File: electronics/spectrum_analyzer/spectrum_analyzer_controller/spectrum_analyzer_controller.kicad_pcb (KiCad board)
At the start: 2 copper layers, 99.1 x 66 mm, 50 parts, among them J1 AudioJack3, J2 Conn_02x03_Odd_Even, J3 Barrel_Jack_Switch, J4 Conn_01x10_Socket, J5 Conn_01x14_Socket, SW1 SW_SPDT, U1 MSGEQ7 MSGEQ7, U2 MSGEQ7 MSGEQ7, U3 ATtiny84 ATtiny84-20P, U4 74HC595 74HC595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

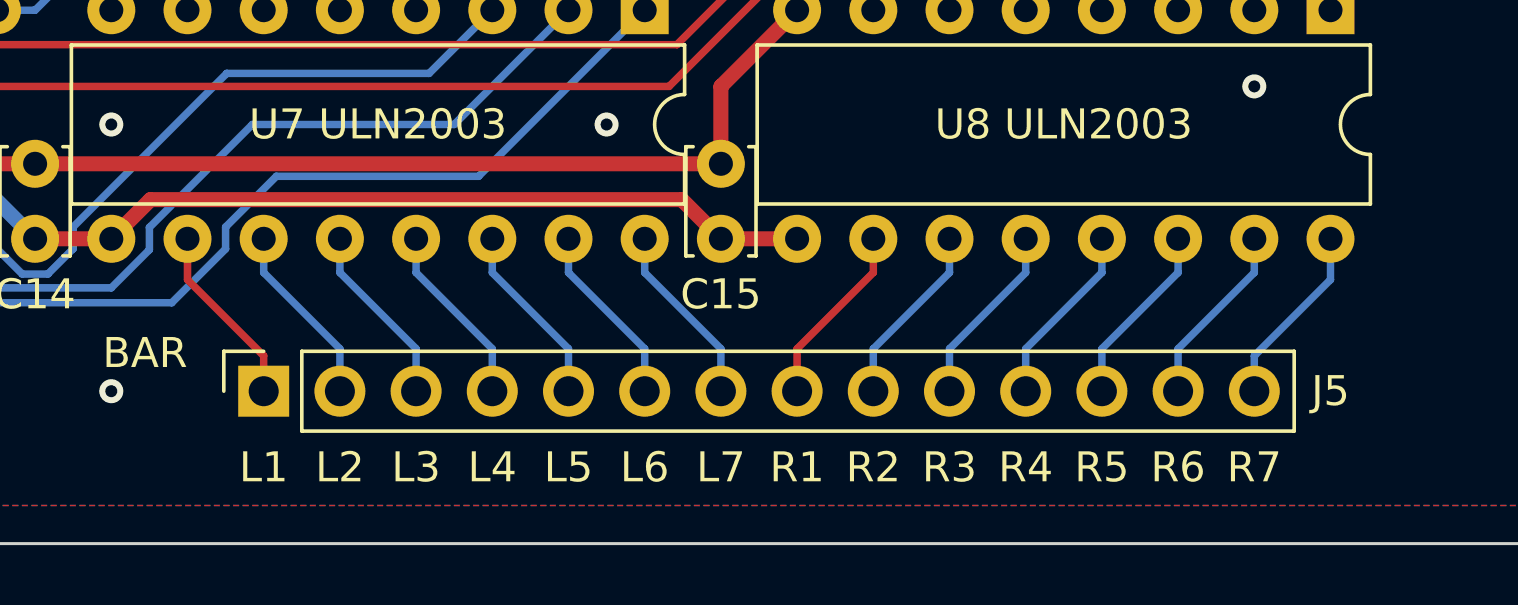
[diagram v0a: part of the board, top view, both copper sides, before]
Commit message: feat: change wire width
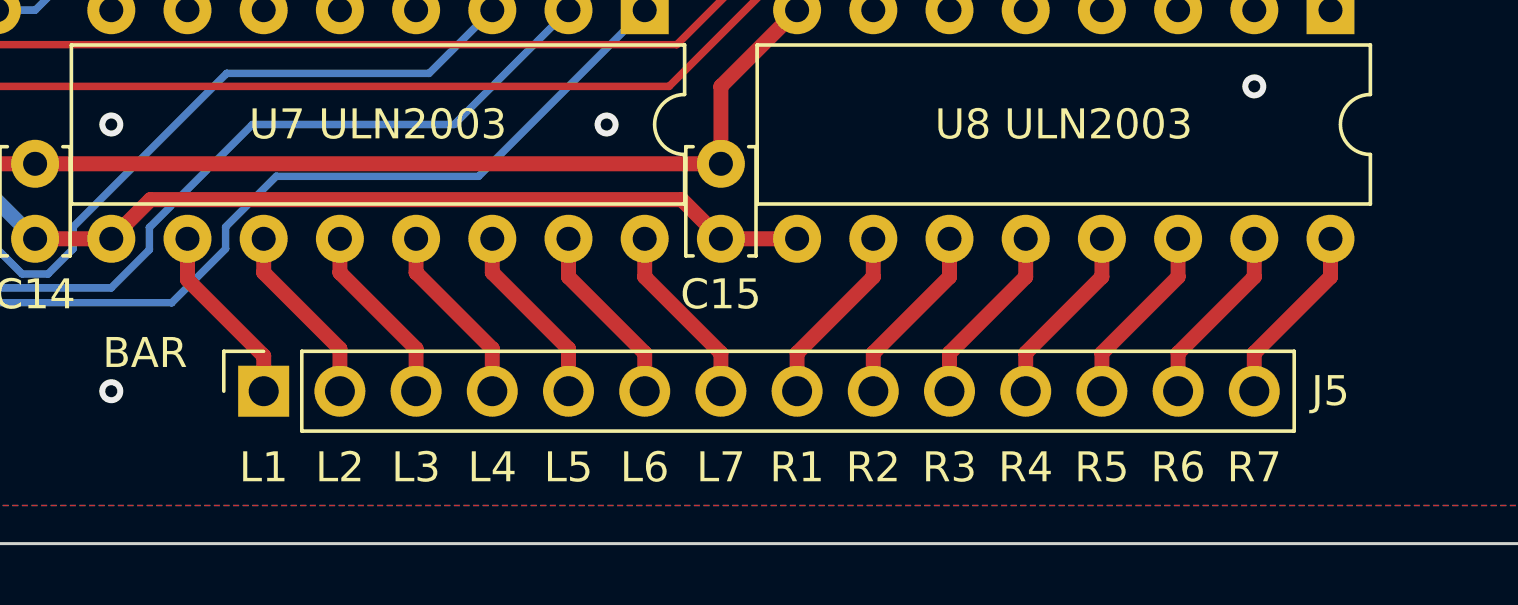
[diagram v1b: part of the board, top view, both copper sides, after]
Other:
- board text added: "Designed by shimo8810 repository: https://github.com/shimo8810/spectrum-analyzer Icon is made by Ehtisham Abid from www.flaticon.com"
- board text removed: "Equalizer icon is made by Ehtisham Abid from www.flaticon.com"
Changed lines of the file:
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@@
   (paper "A5")
   (title_block
+    (title "Spectrum Analyzer Controller")
     (date "2023-08-01")
+    (rev "v0.1.0")
+    (company "shimo8810")
   )
   (layers
@@
       (dashed_line_gap_ratio 3.000000)
       (svgprecision 4)
-      (plotframeref false)
+      (plotframeref true)
       (viasonmask false)
       (mode 1)
@@
       (sketchpadsonfab false)
       (subtractmaskfromsilk false)
-      (outputformat 1)
+      (outputformat 4)
       (mirror false)
-      (drillshape 1)
+      (drillshape 0)
       (scaleselection 1)
       (outputdirectory "")
@@
         (effects (font (size 1 1) (thickness 0.15)))
     )
-    (fp_text value "MountingHole_3.2mm_M3" (at 0 4.2) (layer "F.Fab")
+    (fp_text value "MountingHole_3.2mm_M3" (at 0 -5.08) (layer "F.Fab")
         (effects (font (size 1 1) (thickness 0.15)))
     )
@@
   (gr_rect (start 52.324 29.464) (end 158.496 102.616)
     (stroke (width 0.15) (type default)) (fill none) (layer "User.2"))
-  (gr_text "Equalizer icon is made by Ehtisham Abid from www.flaticon.com" (at 100.33 97.79) (layer "B.SilkS")
-    (effects (font (size 0.75 0.75) (thickness 0.125)) (justify left bottom mirror))
+  (gr_text "Designed by shimo8810\nrepository: https://github.com/shimo8810/spectrum-analyzer\n\nIcon is made by Ehtisham Abid from www.flaticon.com" (at 111.76 45.72) (layer "B.SilkS")
+    (effects (font (size 1 1) (thickness 0.125)) (justify left bottom mirror))
   )
   (gr_text "R5" (at 119.38 96.52) (layer "F.SilkS")
@@
   (segment (start 111.4465 77.3269) (end 104.9534 83.82) (width 0.25) (layer "F.Cu") (net 35))
   (segment (start 119.38 76.2) (end 118.2531 77.3269) (width 0.25) (layer "F.Cu") (net 35))
-  (segment (start 91.44 90.0269) (end 93.98 92.5669) (width 0.25) (layer "B.Cu") (net 36))
-  (segment (start 93.98 92.5669) (end 93.98 93.98) (width 0.25) (layer "B.Cu") (net 36))
-  (segment (start 91.44 88.9) (end 91.44 90.0269) (width 0.25) (layer "B.Cu") (net 36))
-  (segment (start 96.52 88.9) (end 96.52 90.0269) (width 0.25) (layer "B.Cu") (net 37))
-  (segment (start 96.52 90.0269) (end 99.06 92.5669) (width 0.25) (layer "B.Cu") (net 37))
-  (segment (start 99.06 92.5669) (end 99.06 93.98) (width 0.25) (layer "B.Cu") (net 37))
-  (segment (start 101.6 90.0269) (end 104.14 92.5669) (width 0.25) (layer "B.Cu") (net 38))
-  (segment (start 101.6 88.9) (end 101.6 90.0269) (width 0.25) (layer "B.Cu") (net 38))
-  (segment (start 104.14 92.5669) (end 104.14 93.98) (width 0.25) (layer "B.Cu") (net 38))
-  (segment (start 111.76 90.0269) (end 109.22 92.5669) (width 0.25) (layer "F.Cu") (net 39))
-  (segment (start 109.22 92.5669) (end 109.22 93.98) (width 0.25) (layer "F.Cu") (net 39))
-  (segment (start 111.76 88.9) (end 111.76 90.0269) (width 0.25) (layer "F.Cu") (net 39))
-  (segment (start 116.84 90.0269) (end 114.3 92.5669) (width 0.25) (layer "B.Cu") (net 40))
-  (segment (start 116.84 88.9) (end 116.84 90.0269) (width 0.25) (layer "B.Cu") (net 40))
-  (segment (start 114.3 92.5669) (end 114.3 93.98) (width 0.25) (layer "B.Cu") (net 40))
-  (segment (start 121.92 90.0269) (end 119.38 92.5669) (width 0.25) (layer "B.Cu") (net 41))
-  (segment (start 121.92 88.9) (end 121.92 90.0269) (width 0.25) (layer "B.Cu") (net 41))
-  (segment (start 119.38 92.5669) (end 119.38 93.98) (width 0.25) (layer "B.Cu") (net 41))
-  (segment (start 124.46 93.98) (end 124.46 92.8031) (width 0.25) (layer "B.Cu") (net 42))
-  (segment (start 127 88.9) (end 127 90.2631) (width 0.25) (layer "B.Cu") (net 42))
-  (segment (start 127 90.2631) (end 124.46 92.8031) (width 0.25) (layer "B.Cu") (net 42))
-  (segment (start 91.44 93.98) (end 91.44 92.8031) (width 0.25) (layer "F.Cu") (net 43))
-  (segment (start 88.9 90.2631) (end 91.44 92.8031) (width 0.25) (layer "F.Cu") (net 43))
-  (segment (start 88.9 88.9) (end 88.9 90.2631) (width 0.25) (layer "F.Cu") (net 43))
-  (segment (start 96.52 92.5669) (end 93.98 90.0269) (width 0.25) (layer "B.Cu") (net 44))
-  (segment (start 96.52 93.98) (end 96.52 92.5669) (width 0.25) (layer "B.Cu") (net 44))
-  (segment (start 93.98 88.9) (end 93.98 90.0269) (width 0.25) (layer "B.Cu") (net 44))
-  (segment (start 101.6 92.5669) (end 99.06 90.0269) (width 0.25) (layer "B.Cu") (net 45))
-  (segment (start 99.06 88.9) (end 99.06 90.0269) (width 0.25) (layer "B.Cu") (net 45))
-  (segment (start 101.6 93.98) (end 101.6 92.5669) (width 0.25) (layer "B.Cu") (net 45))
-  (segment (start 106.68 92.5669) (end 104.14 90.0269) (width 0.25) (layer "B.Cu") (net 46))
-  (segment (start 104.14 88.9) (end 104.14 90.0269) (width 0.25) (layer "B.Cu") (net 46))
-  (segment (start 106.68 93.98) (end 106.68 92.5669) (width 0.25) (layer "B.Cu") (net 46))
-  (segment (start 111.76 92.5669) (end 111.76 93.98) (width 0.25) (layer "B.Cu") (net 47))
-  (segment (start 114.3 90.0269) (end 111.76 92.5669) (width 0.25) (layer "B.Cu") (net 47))
-  (segment (start 114.3 88.9) (end 114.3 90.0269) (width 0.25) (layer "B.Cu") (net 47))
-  (segment (start 119.38 90.0269) (end 116.84 92.5669) (width 0.25) (layer "B.Cu") (net 48))
-  (segment (start 119.38 88.9) (end 119.38 90.0269) (width 0.25) (layer "B.Cu") (net 48))
-  (segment (start 116.84 92.5669) (end 116.84 93.98) (width 0.25) (layer "B.Cu") (net 48))
-  (segment (start 124.46 88.9) (end 124.46 90.0269) (width 0.25) (layer "B.Cu") (net 49))
-  (segment (start 124.46 90.0269) (end 121.92 92.5669) (width 0.25) (layer "B.Cu") (net 49))
-  (segment (start 121.92 92.5669) (end 121.92 93.98) (width 0.25) (layer "B.Cu") (net 49))
+  (segment (start 91.44 90.0269) (end 93.98 92.5669) (width 0.5) (layer "F.Cu") (net 36))
+  (segment (start 93.98 92.5669) (end 93.98 93.98) (width 0.5) (layer "F.Cu") (net 36))
+  (segment (start 91.44 88.9) (end 91.44 90.0269) (width 0.5) (layer "F.Cu") (net 36))
+  (segment (start 96.52 88.9) (end 96.52 90.0269) (width 0.5) (layer "F.Cu") (net 37))
+  (segment (start 96.52 90.0269) (end 99.06 92.5669) (width 0.5) (layer "F.Cu") (net 37))
+  (segment (start 99.06 92.5669) (end 99.06 93.98) (width 0.5) (layer "F.Cu") (net 37))
+  (segment (start 101.6 90.17) (end 104.14 92.71) (width 0.5) (layer "F.Cu") (net 38))
+  (segment (start 101.6 88.9) (end 101.6 90.17) (width 0.5) (layer "F.Cu") (net 38))
+  (segment (start 104.14 92.71) (end 104.14 93.98) (width 0.5) (layer "F.Cu") (net 38))
+  (segment (start 111.76 88.9) (end 111.76 90.17) (width 0.5) (layer "F.Cu") (net 39))
+  (segment (start 109.22 92.71) (end 109.22 93.98) (width 0.5) (layer "F.Cu") (net 39))
+  (segment (start 111.76 90.17) (end 109.22 92.71) (width 0.5) (layer "F.Cu") (net 39))
+  (segment (start 116.84 90.17) (end 114.3 92.71) (width 0.5) (layer "F.Cu") (net 40))
+  (segment (start 114.3 92.71) (end 114.3 93.98) (width 0.5) (layer "F.Cu") (net 40))
+  (segment (start 116.84 88.9) (end 116.84 90.17) (width 0.5) (layer "F.Cu") (net 40))
+  (segment (start 119.38 92.71) (end 119.38 93.98) (width 0.5) (layer "F.Cu") (net 41))
+  (segment (start 121.92 90.17) (end 119.38 92.71) (width 0.5) (layer "F.Cu") (net 41))
+  (segment (start 121.92 88.9) (end 121.92 90.17) (width 0.5) (layer "F.Cu") (net 41))
+  (segment (start 127 90.17) (end 124.46 92.71) (width 0.5) (layer "F.Cu") (net 42))
+  (segment (start 127 88.9) (end 127 90.17) (width 0.5) (layer "F.Cu") (net 42))
+  (segment (start 124.46 92.71) (end 124.46 93.98) (width 0.5) (layer "F.Cu") (net 42))
+  (segment (start 91.44 93.98) (end 91.44 92.8031) (width 0.5) (layer "F.Cu") (net 43))
+  (segment (start 88.9 90.2631) (end 91.44 92.8031) (width 0.5) (layer "F.Cu") (net 43))
+  (segment (start 88.9 88.9) (end 88.9 90.2631) (width 0.5) (layer "F.Cu") (net 43))
+  (segment (start 96.52 92.5669) (end 93.98 90.0269) (width 0.5) (layer "F.Cu") (net 44))
+  (segment (start 96.52 93.98) (end 96.52 92.5669) (width 0.5) (layer "F.Cu") (net 44))
+  (segment (start 93.98 88.9) (end 93.98 90.0269) (width 0.5) (layer "F.Cu") (net 44))
+  (segment (start 101.6 92.5669) (end 99.06 90.0269) (width 0.5) (layer "F.Cu") (net 45))
+  (segment (start 99.06 88.9) (end 99.06 90.0269) (width 0.5) (layer "F.Cu") (net 45))
+  (segment (start 101.6 93.98) (end 101.6 92.5669) (width 0.5) (layer "F.Cu") (net 45))
+  (segment (start 104.14 90.17) (end 106.68 92.71) (width 0.5) (layer "F.Cu") (net 46))
+  (segment (start 104.14 88.9) (end 104.14 90.17) (width 0.5) (layer "F.Cu") (net 46))
+  (segment (start 106.68 92.71) (end 106.68 93.98) (width 0.5) (layer "F.Cu") (net 46))
+  (segment (start 114.3 88.9) (end 114.3 90.17) (width 0.5) (layer "F.Cu") (net 47))
+  (segment (start 114.3 90.17) (end 111.76 92.71) (width 0.5) (layer "F.Cu") (net 47))
+  (segment (start 111.76 92.71) (end 111.76 93.98) (width 0.5) (layer "F.Cu") (net 47))
+  (segment (start 119.38 88.9) (end 119.38 90.17) (width 0.5) (layer "F.Cu") (net 48))
+  (segment (start 116.84 92.71) (end 116.84 93.98) (width 0.5) (layer "F.Cu") (net 48))
+  (segment (start 119.38 90.17) (end 116.84 92.71) (width 0.5) (layer "F.Cu") (net 48))
+  (segment (start 124.46 88.9) (end 124.46 90.17) (width 0.5) (layer "F.Cu") (net 49))
+  (segment (start 124.46 90.17) (end 121.92 92.71) (width 0.5) (layer "F.Cu") (net 49))
+  (segment (start 121.92 92.71) (end 121.92 93.98) (width 0.5) (layer "F.Cu") (net 49))
   (segment (start 140.9284 44.4916) (end 139.7 45.72) (width 0.25) (layer "B.Cu") (net 50))
   (segment (start 140.9284 39.3284) (end 140.9284 44.4916) (width 0.25) (layer "B.Cu") (net 50))

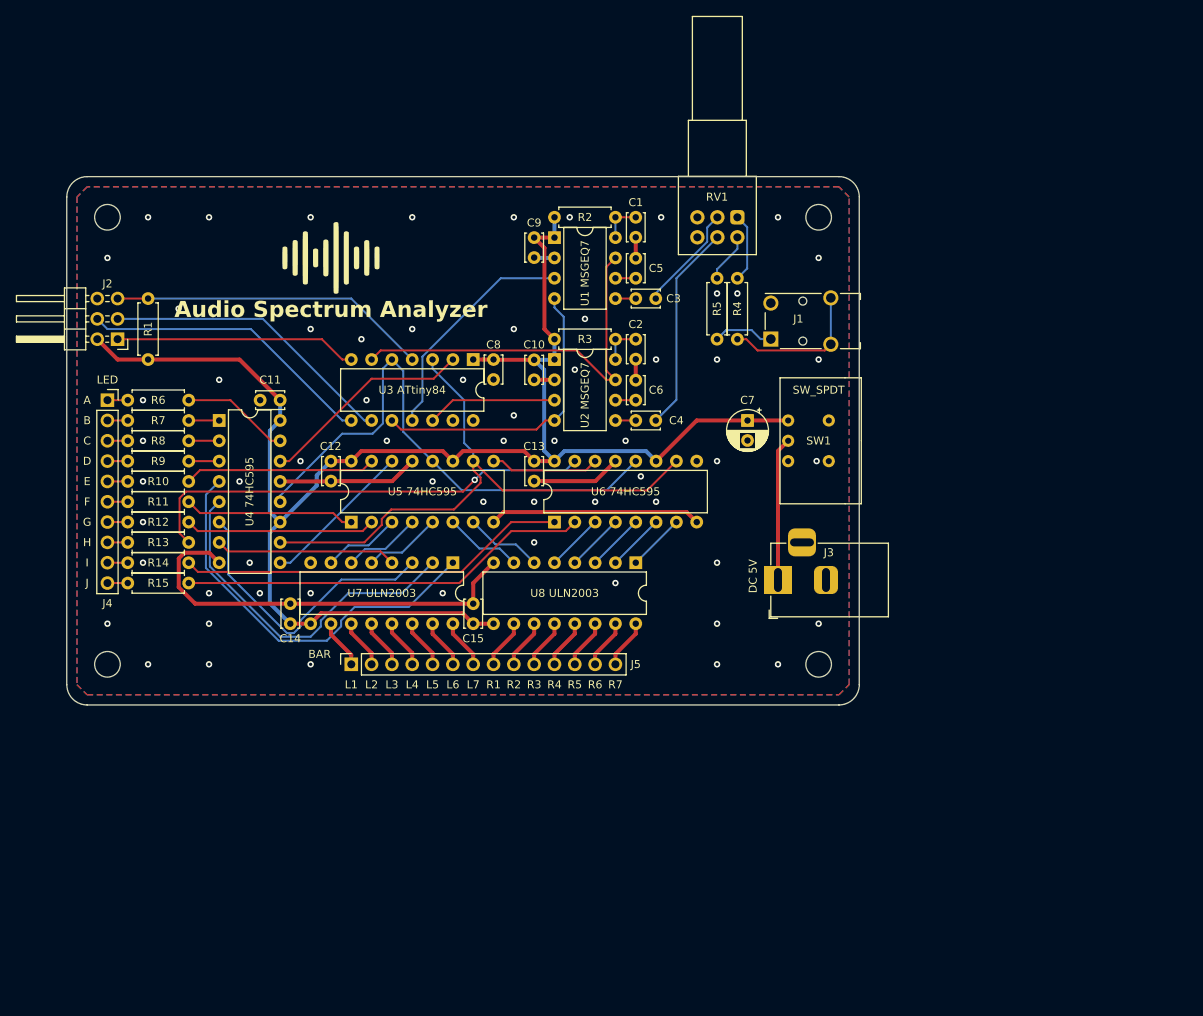
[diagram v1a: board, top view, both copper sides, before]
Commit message: feat: change pcb layout and enclosure design
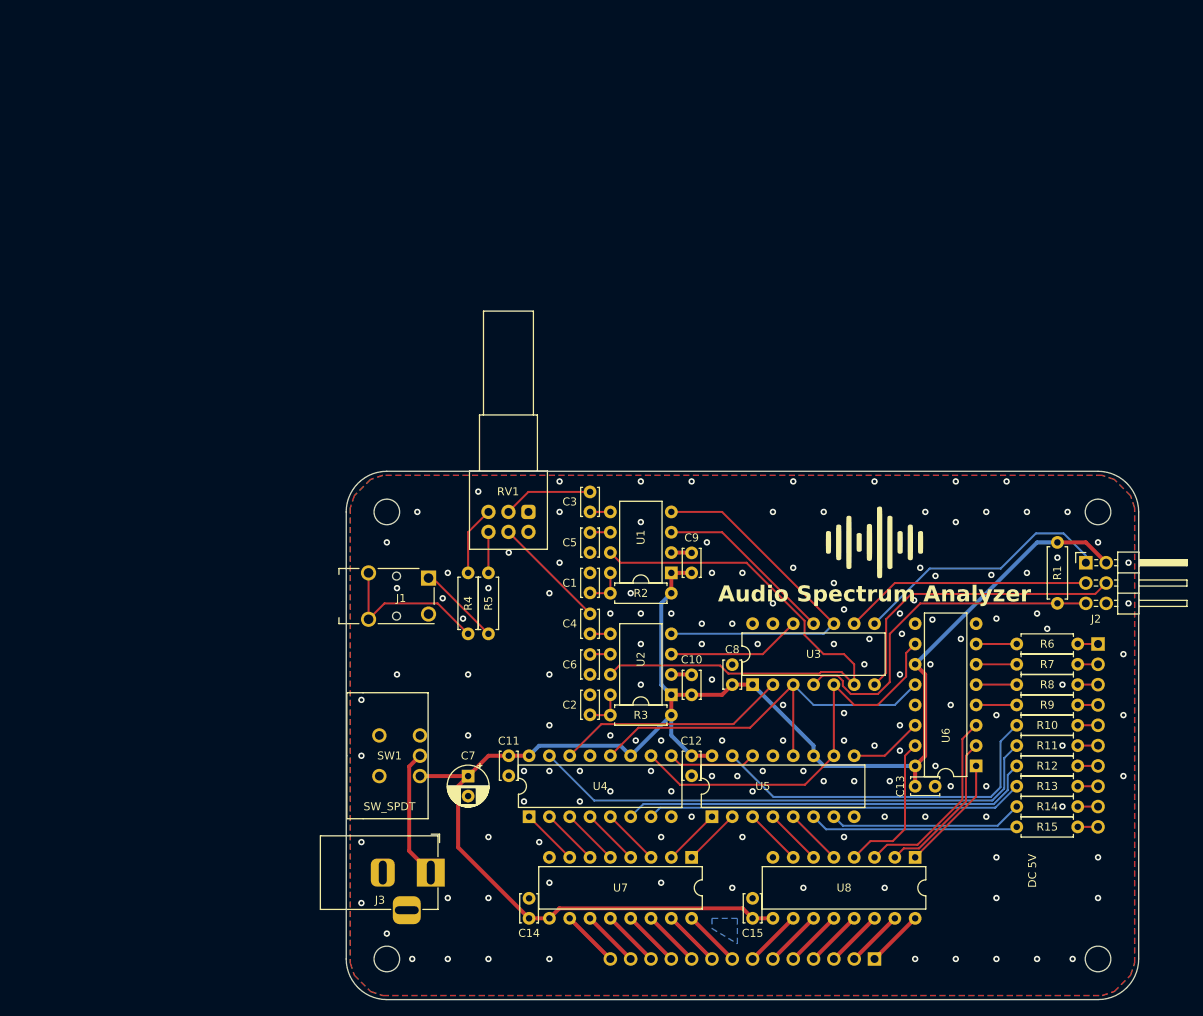
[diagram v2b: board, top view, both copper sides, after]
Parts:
- J4, J5: moved to B.Cu
- U1: renamed from U1 MSGEQ7
- U2: renamed from U2 MSGEQ7
- U3: renamed from U3 ATtiny84
- U4: renamed from U4 74HC595
- U5: renamed from U5 74HC595
- U6: renamed from U6 74HC595
- U7: renamed from U7 ULN2003
- U8: renamed from U8 ULN2003
- moved J4 127.5 mm to (184.8, 91.4), turned to 180 degrees
- moved J2 124.2 mm to (183.3, 81.3), turned to 0 degrees
- moved R1 115.9 mm to (179.7, 78.7), turned to -90 degrees
- moved R10 107.9 mm to (174.6, 101.6), turned to 0 degrees
- moved R11 107.9 mm to (174.6, 104.1), turned to 0 degrees
- moved R12 107.9 mm to (174.6, 106.7), turned to 0 degrees
- moved R13 107.9 mm to (174.6, 109.2), turned to 0 degrees
- moved R14 107.9 mm to (174.6, 111.8), turned to 0 degrees
- moved R15 107.9 mm to (174.6, 114.3), turned to 0 degrees
- moved R6 107.9 mm to (174.6, 91.4), turned to 0 degrees
- moved R7 107.9 mm to (174.6, 94.0), turned to 0 degrees
- moved R8 107.9 mm to (174.6, 96.5), turned to 0 degrees
- moved R9 107.9 mm to (174.6, 99.1), turned to 0 degrees
- moved G1 76.7 mm to (156.8, 78.7)
- moved J5 75.1 mm to (156.8, 130.8)
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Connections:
- net Net-(SW1-B) renamed VDC
- J2 pad 1: /ICSP_MOSI -> /ICSP_MISO
- J2 pad 4: /ICSP_MISO -> /ICSP_MOSI
- J5 pad 1: /RIGHT_1 -> /LEFT_1
- J5 pad 13: /RIGHT_7 -> /LEFT_7
- J5 pad 14: /LEFT_7 -> /RIGHT_7
- J5 pad 2: /LEFT_1 -> /RIGHT_1
- RV1 pad 1: Net-(R4-Pad1) -> GND
- RV1 pad 3: GND -> Net-(R4-Pad1)
- RV1 pad 4: Net-(R5-Pad2) -> GND
- RV1 pad 6: GND -> Net-(R5-Pad2)
- U3 pad 3: /LED_CLOCK -> /LED_LATCH
- U3 pad 5: /LED_LATCH -> /LED_CLOCK
- U4 pad 1: /LED_B -> Net-(U4-QB)
- U4 pad 15: /LED_A -> /LED_F
- U4 pad 2: /LED_C -> Net-(U4-QC)
- U4 pad 3: /LED_D -> Net-(U4-QD)
- U4 pad 6: Net-(U4-QG) -> /LED_G
- U4 pad 7: Net-(U4-QH) -> /LED_H
- U5 pad 1: /LED_F -> Net-(U5-QB)
- U5 pad 2: /LED_G -> Net-(U5-QC)
- U5 pad 6: Net-(U5-QG) -> /LED_J
- U5 pad 7: Net-(U5-QH) -> /LED_I
- U6 pad 1: /LED_I -> Net-(U6-QB)
- U6 pad 15: /LED_H -> Net-(U6-QA)
- U6 pad 2: /LED_J -> Net-(U6-QC)
- U6 pad 4: Net-(U6-QE) -> /LED_D
- U6 pad 5: Net-(U6-QF) -> /LED_C
- U6 pad 6: Net-(U6-QG) -> /LED_B
- U6 pad 7: Net-(U6-QH) -> /LED_A
- U7 pad 1: Net-(U4-QE) -> Net-(U5-QC)
- U7 pad 10: /RIGHT_1 -> /RIGHT_7
- U7 pad 11: /LEFT_1 -> /LEFT_7
- U7 pad 12: /RIGHT_2 -> /LEFT_6
- U7 pad 13: /LEFT_2 -> /RIGHT_6
- U7 pad 14: /RIGHT_3 -> /LEFT_5
- U7 pad 15: /LEFT_3 -> /RIGHT_5
- U7 pad 16: /RIGHT_4 -> /LEFT_4
- U7 pad 2: Net-(U4-QF) -> Net-(U5-QB)
- U7 pad 3: Net-(U4-QG) -> Net-(U4-QF)
- U7 pad 4: Net-(U4-QH) -> Net-(U4-QE)
- U7 pad 5: Net-(U5-QF) -> Net-(U4-QD)
- U7 pad 6: Net-(U5-QE) -> Net-(U4-QC)
- U7 pad 7: Net-(U5-QD) -> Net-(U4-QB)
- U8 pad 1: Net-(U6-QH) -> Net-(U6-QB)
- U8 pad 10: /LEFT_4 -> /RIGHT_4
- U8 pad 11: /RIGHT_5 -> /LEFT_3
- U8 pad 12: /LEFT_5 -> /RIGHT_3
- U8 pad 13: /RIGHT_6 -> /LEFT_2
- U8 pad 14: /LEFT_6 -> /RIGHT_2
- U8 pad 15: /RIGHT_7 -> /RIGHT_1
- U8 pad 16: /LEFT_7 -> /LEFT_1
- U8 pad 2: Net-(U6-QG) -> Net-(U6-QC)
- U8 pad 3: Net-(U6-QF) -> Net-(U6-QD)
- U8 pad 4: Net-(U6-QE) -> Net-(U6-QA)
- U8 pad 5: Net-(U6-QD) -> Net-(U5-QF)
- U8 pad 6: Net-(U5-QH) -> Net-(U5-QE)
- U8 pad 7: Net-(U5-QG) -> Net-(U5-QD)
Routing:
- net GND: track 118.8 -> 5.11 mm, vias 62 -> 143
- net /LED_F: track 21.4 -> 65.8 mm
- net Net-(U4-QE): track 50.6 -> 7.18 mm
- net Net-(U4-QF): track 44.3 -> 7.18 mm
- net Net-(U4-QG): track 37.1 -> 0.00 mm
- net /LED_G: track 23.8 -> 52.0 mm
- net /LED_J: track 51.4 -> 26.2 mm
- net /LED_I: track 48.8 -> 24.3 mm
- net /LED_CLOCK: track 74.9 -> 50.8 mm
- net /GEQ_RESET: track 48.6 -> 72.0 mm
- net Net-(U4-QH): track 22.6 -> 0.00 mm
- net /LED_E: track 23.9 -> 44.7 mm
- net Net-(U6-QC): track 0.00 -> 19.3 mm
- net Net-(U6-QA): track 0.00 -> 18.8 mm
- net Net-(U6-QD): track 7.18 -> 24.0 mm
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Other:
- outline, holes or cut-outs redrawn
- board text added: "Designed by shimo8810 https://github.com/shimo8810/spectrum-analyzer Equalizer icons created by Ehtisham Abid - Flaticon"
